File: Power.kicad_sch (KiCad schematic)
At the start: 23 parts, among them J201 Barrel_Jack, U201 LM2576HVT-5, U202 LM7815_TO220, U203 MC34063AP, U204 LM7905_TO220

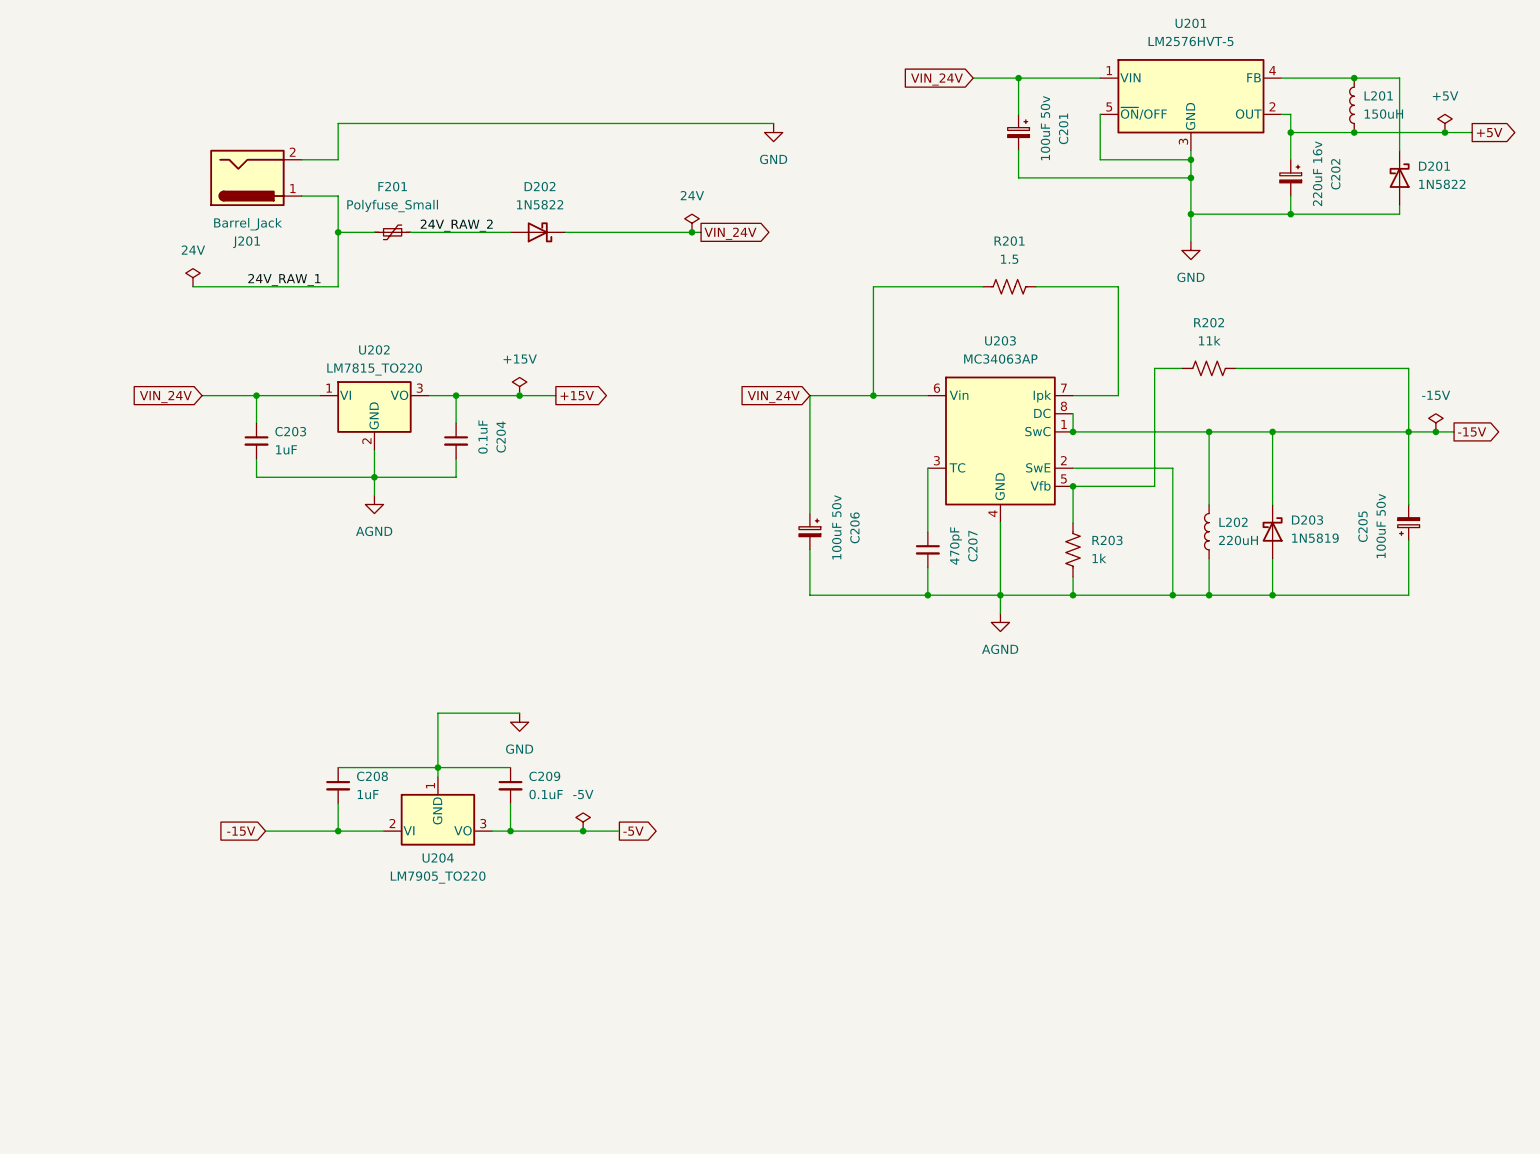
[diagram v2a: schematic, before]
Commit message: Added Datasheets and specified polyfuse parameters.
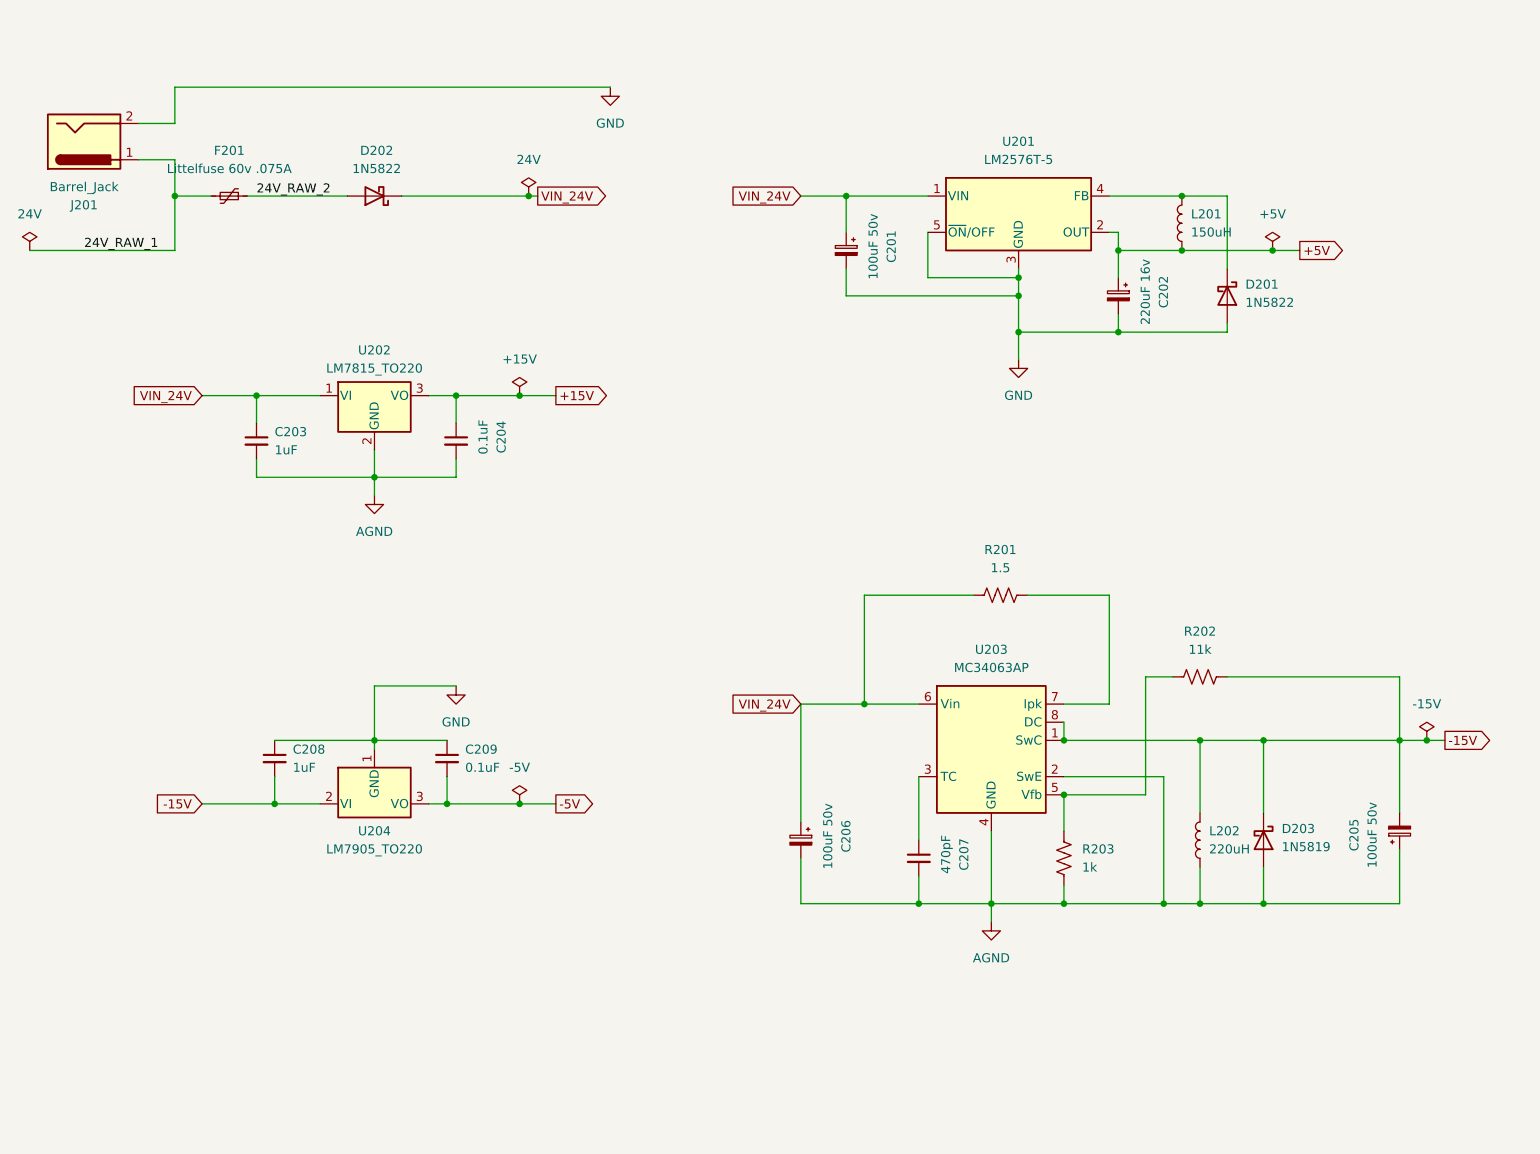
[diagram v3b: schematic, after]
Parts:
- removed U201: LM2576HVT-5, Package_TO_SOT_THT:TO-220-5_Vertical, symbol Regulator_Switching:LM2576HVT-5
- added U201: LM2576T-5, Package_TO_SOT_THT:TO-220-5_Vertical, symbol Regulator_Switching:LM2576T-5
- F201: value Polyfuse_Small -> Littelfuse 60v .075A
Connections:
- net +5V: now also U201.2 (OUT)
- net GND: now also U201.3 (GND), U201.5 (~{ON}/OFF)
- net VIN_24V: now also U201.1 (VIN)
- net at D201.1 (K), L201.2: now also U201.4 (FB)
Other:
- moved on the sheet: C201, C202, C205, C206, C207, C208, C209, D201, D202, D203, F201, J201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
